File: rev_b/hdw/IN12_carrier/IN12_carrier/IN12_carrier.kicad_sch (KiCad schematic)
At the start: 0 parts

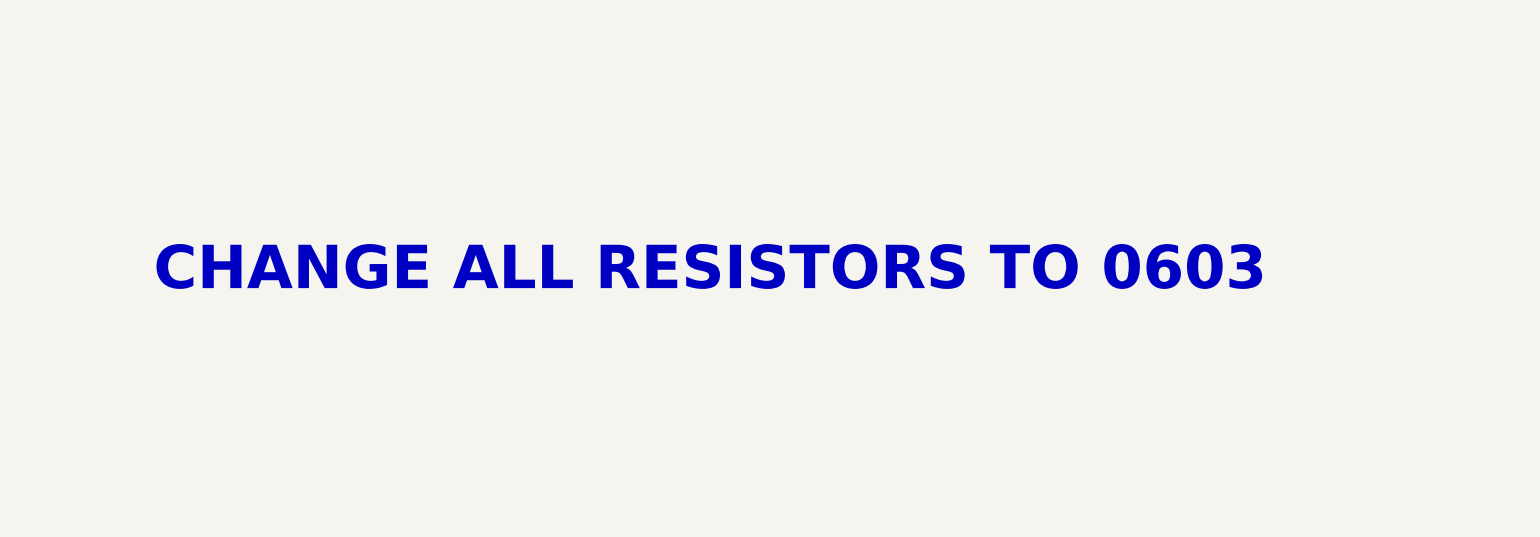
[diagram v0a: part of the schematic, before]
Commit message: updated footprints, ran some DRC
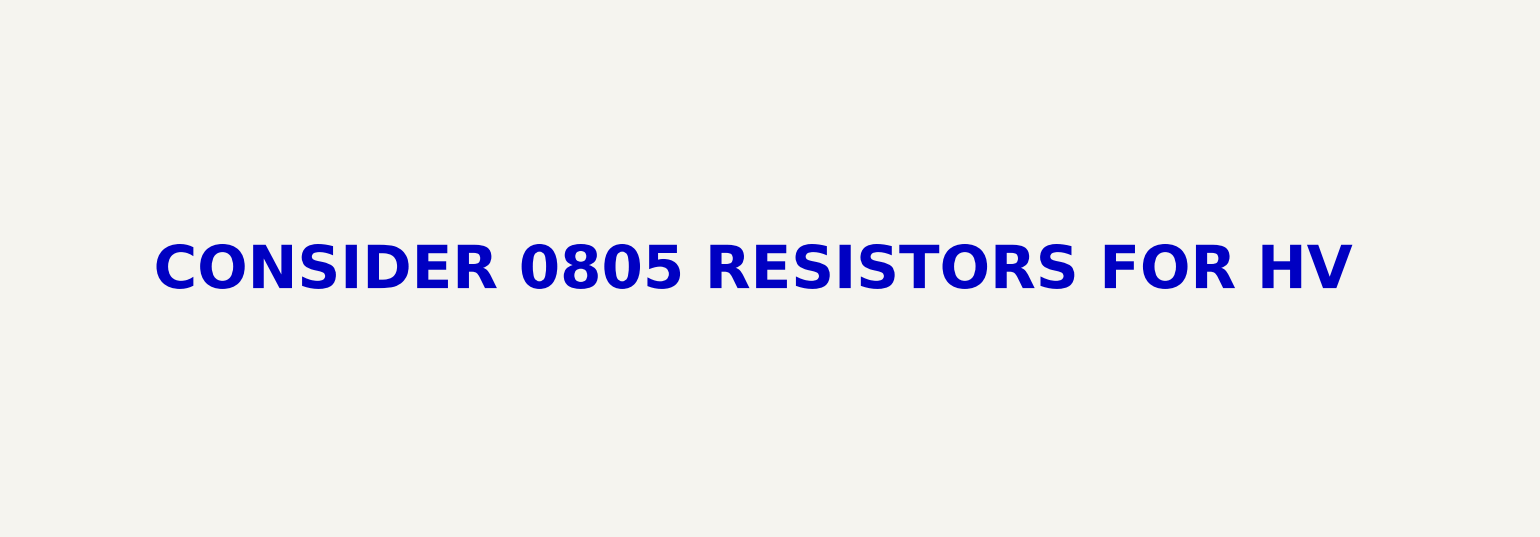
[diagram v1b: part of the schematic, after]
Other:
- note added: "CONSIDER 0805 RESISTORS FOR HV"
- note removed: "CHANGE ALL RESISTORS TO 0603"
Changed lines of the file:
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@@
     (company "Drew Maatman")
   )
-  (text "CHANGE ALL RESISTORS TO 0603" (at 121.92 52.07 0)
+  (text "CONSIDER 0805 RESISTORS FOR HV" (at 121.92 52.07 0)
     (effects (font (face "Courier New") (size 5.08 5.08) (thickness 1.016) bold (color 194 0 0 1)) (justify left bottom))
   )

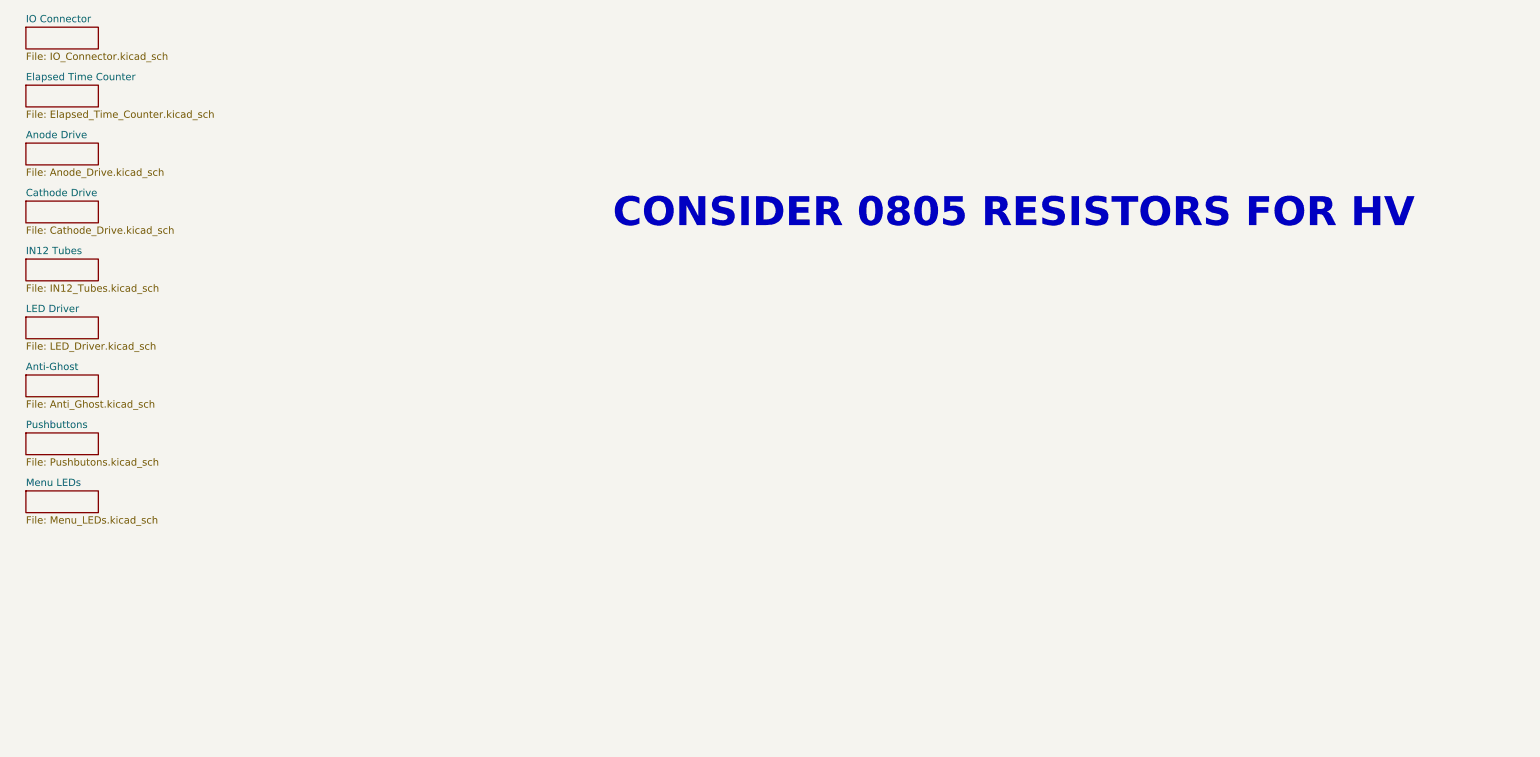
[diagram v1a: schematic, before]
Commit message: annotated, started arranging parts for IN12 carrier
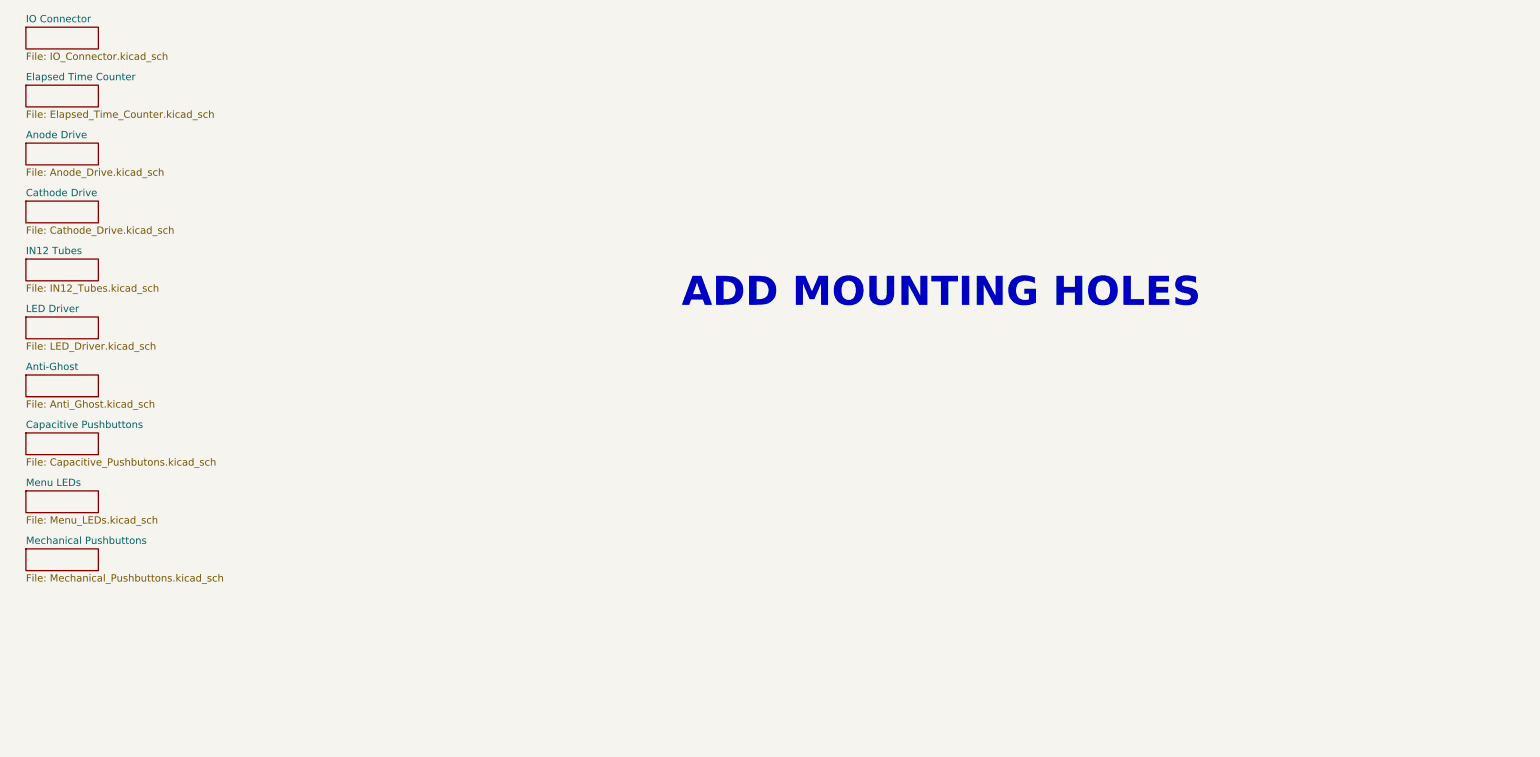
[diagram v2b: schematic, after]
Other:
- sheet Pushbuttons renamed Capacitive Pushbuttons
- added sheet Mechanical Pushbuttons (Mechanical_Pushbuttons.kicad_sch)
- sheet Capacitive Pushbuttons: file Pushbutons.kicad_sch -> Capacitive_Pushbutons.kicad_sch
- note added: "ADD MOUNTING HOLES"
- note removed: "CONSIDER 0805 RESISTORS FOR HV"
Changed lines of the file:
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@@
     (company "Drew Maatman")
   )
-  (text "CONSIDER 0805 RESISTORS FOR HV" (at 121.92 52.07 0)
-    (effects (font (face "Courier New") (size 5.08 5.08) (thickness 1.016) bold (color 194 0 0 1)) (justify left bottom))
+  (text "ADD MOUNTING HOLES" (at 133.985 66.04 0)
+    (effects (font (face "Courier New") (size 5.08 5.08) (thickness 1.016) bold (color 255 0 0 1)) (justify left bottom))
   )
   (sheet (at 19.05 46.99) (size 12.7 3.81) (fields_autoplaced)
@@
     (stroke (width 0.1524) (type solid))
     (fill (color 0 0 0 0.0000))
-    (property "Sheetname" "Pushbuttons" (at 19.05 86.9184 0)
+    (property "Sheetname" "Capacitive Pushbuttons" (at 19.05 86.9184 0)
       (effects (font (size 1.27 1.27)) (justify left bottom))
     )
-    (property "Sheetfile" "Pushbutons.kicad_sch" (at 19.05 92.0246 0)
+    (property "Sheetfile" "Capacitive_Pushbutons.kicad_sch" (at 19.05 92.0246 0)
       (effects (font (size 1.27 1.27)) (justify left top))
     )
@@
       )
     )
+  )
+  (sheet (at 19.05 107.95) (size 12.7 3.81) (fields_autoplaced)
+    (stroke (width 0.1524) (type solid))
+    (fill (color 0 0 0 0.0000))
+    (property "Sheetname" "Mechanical Pushbuttons" (at 19.05 107.2384 0)
+      (effects (font (size 1.27 1.27)) (justify left bottom))
+    )
+    (property "Sheetfile" "Mechanical_Pushbuttons.kicad_sch" (at 19.05 112.3446 0)
+      (effects (font (size 1.27 1.27)) (justify left top))
+    )
+    (instances
+      (project "IN12_carrier"
+        (path "/c4d83a5b-e6ae-4326-9df5-0c4ac01f7d8c" (page "11"))
+      )
+    )

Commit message: lots of placement progress on IN12 carrier board
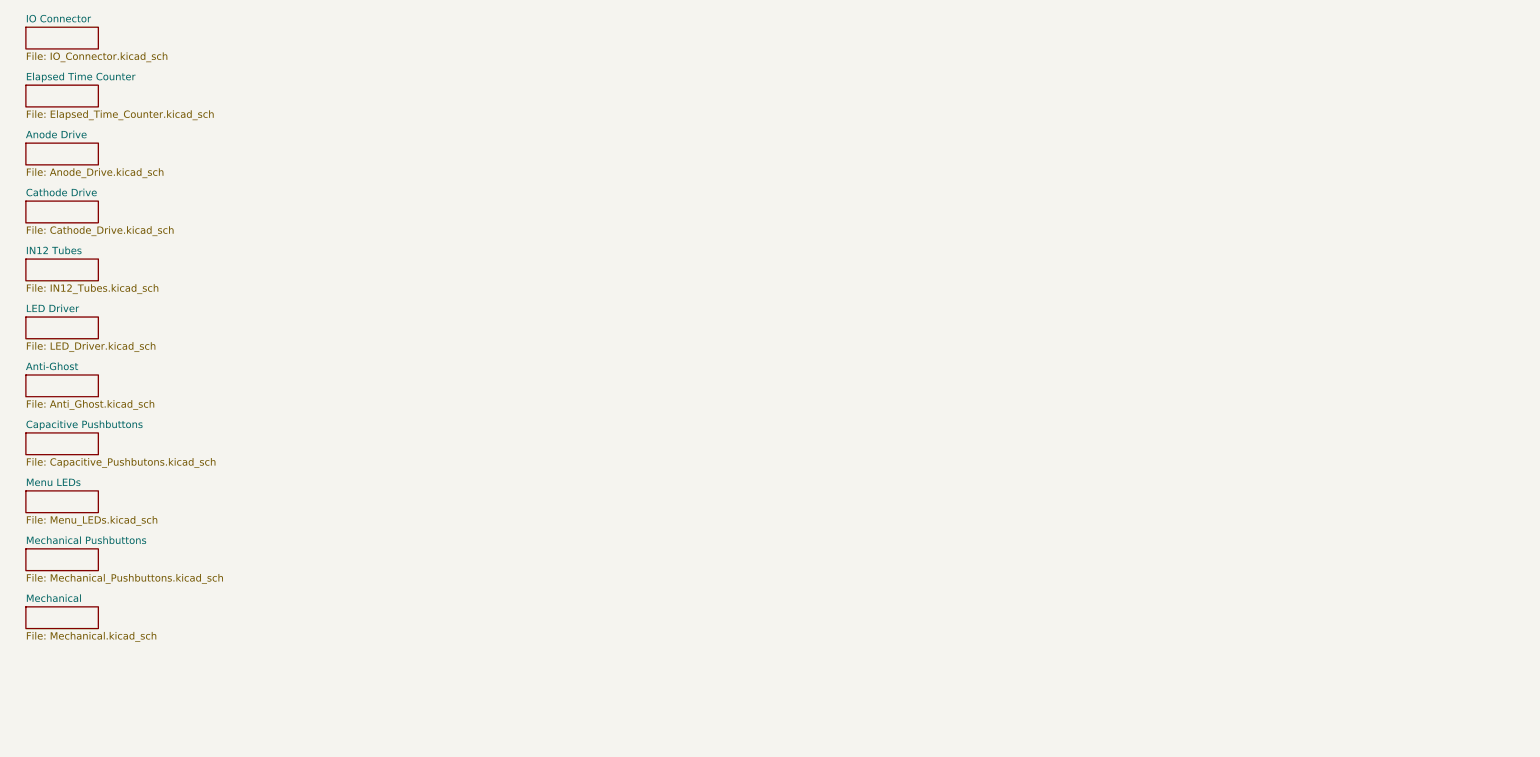
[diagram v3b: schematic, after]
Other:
- added sheet Mechanical (Mechanical.kicad_sch)
- note removed: "ADD MOUNTING HOLES"
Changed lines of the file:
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@@
     (company "Drew Maatman")
-  )
-  (text "ADD MOUNTING HOLES" (at 133.985 66.04 0)
-    (effects (font (face "Courier New") (size 5.08 5.08) (thickness 1.016) bold (color 255 0 0 1)) (justify left bottom))
   )
   (sheet (at 19.05 46.99) (size 12.7 3.81) (fields_autoplaced)
@@
       )
     )
+  )
+  (sheet (at 19.05 118.11) (size 12.7 3.81) (fields_autoplaced)
+    (stroke (width 0.1524) (type solid))
+    (fill (color 0 0 0 0.0000))
+    (property "Sheetname" "Mechanical" (at 19.05 117.3984 0)
+      (effects (font (size 1.27 1.27)) (justify left bottom))
+    )
+    (property "Sheetfile" "Mechanical.kicad_sch" (at 19.05 122.5046 0)
+      (effects (font (size 1.27 1.27)) (justify left top))
+    )
+    (instances
+      (project "IN12_carrier"
+        (path "/c4d83a5b-e6ae-4326-9df5-0c4ac01f7d8c" (page "12"))
+      )
+    )

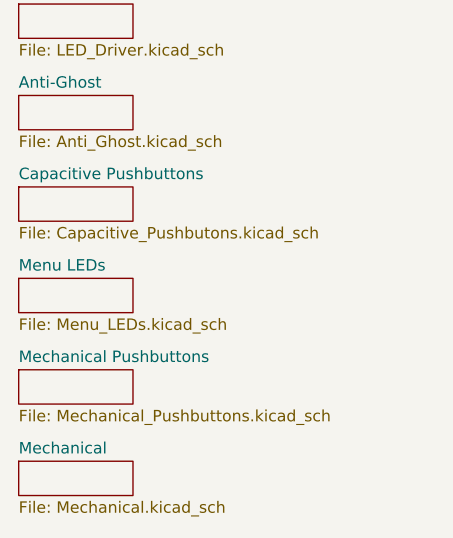
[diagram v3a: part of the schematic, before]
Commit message: lots of routing and design progress on IN12 carrier board
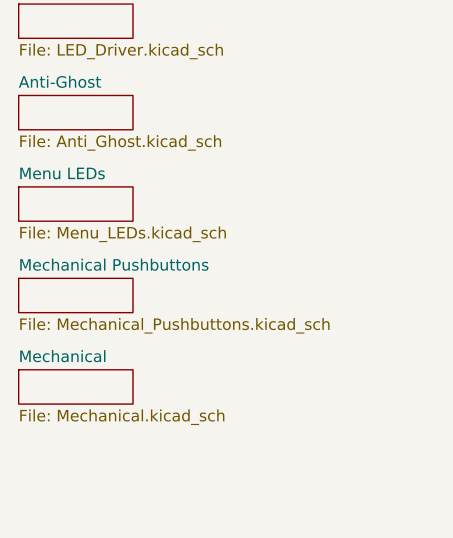
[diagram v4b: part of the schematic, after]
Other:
- removed sheet Capacitive Pushbuttons
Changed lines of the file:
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@@
     )
   )
-  (sheet (at 19.05 118.11) (size 12.7 3.81) (fields_autoplaced)
+  (sheet (at 19.05 107.95) (size 12.7 3.81) (fields_autoplaced)
     (stroke (width 0.1524) (type solid))
     (fill (color 0 0 0 0.0000))
-    (property "Sheetname" "Mechanical" (at 19.05 117.3984 0)
+    (property "Sheetname" "Mechanical" (at 19.05 107.2384 0)
       (effects (font (size 1.27 1.27)) (justify left bottom))
     )
-    (property "Sheetfile" "Mechanical.kicad_sch" (at 19.05 122.5046 0)
+    (property "Sheetfile" "Mechanical.kicad_sch" (at 19.05 112.3446 0)
       (effects (font (size 1.27 1.27)) (justify left top))
     )
@@
     )
   )
-  (sheet (at 19.05 97.79) (size 12.7 3.81) (fields_autoplaced)
+  (sheet (at 19.05 87.63) (size 12.7 3.81) (fields_autoplaced)
     (stroke (width 0.1524) (type solid))
     (fill (color 0 0 0 0.0000))
-    (property "Sheetname" "Menu LEDs" (at 19.05 97.0784 0)
+    (property "Sheetname" "Menu LEDs" (at 19.05 86.9184 0)
       (effects (font (size 1.27 1.27)) (justify left bottom))
     )
-    (property "Sheetfile" "Menu_LEDs.kicad_sch" (at 19.05 102.1846 0)
+    (property "Sheetfile" "Menu_LEDs.kicad_sch" (at 19.05 92.0246 0)
       (effects (font (size 1.27 1.27)) (justify left top))
     )
@@
     )
   )
-  (sheet (at 19.05 87.63) (size 12.7 3.81) (fields_autoplaced)
-    (stroke (width 0.1524) (type solid))
-    (fill (color 0 0 0 0.0000))
-    (property "Sheetname" "Capacitive Pushbuttons" (at 19.05 86.9184 0)
-      (effects (font (size 1.27 1.27)) (justify left bottom))
-    )
-    (property "Sheetfile" "Capacitive_Pushbutons.kicad_sch" (at 19.05 92.0246 0)
-      (effects (font (size 1.27 1.27)) (justify left top))
-    )
-    (instances
-      (project "IN12_carrier"
-        (path "/c4d83a5b-e6ae-4326-9df5-0c4ac01f7d8c" (page "9"))
-      )
-    )
-  )
   (sheet (at 19.05 67.31) (size 12.7 3.81) (fields_autoplaced)
     (stroke (width 0.1524) (type solid))
@@
     )
   )
-  (sheet (at 19.05 107.95) (size 12.7 3.81) (fields_autoplaced)
+  (sheet (at 19.05 97.79) (size 12.7 3.81) (fields_autoplaced)
     (stroke (width 0.1524) (type solid))
     (fill (color 0 0 0 0.0000))
-    (property "Sheetname" "Mechanical Pushbuttons" (at 19.05 107.2384 0)
+    (property "Sheetname" "Mechanical Pushbuttons" (at 19.05 97.0784 0)
       (effects (font (size 1.27 1.27)) (justify left bottom))
     )
-    (property "Sheetfile" "Mechanical_Pushbuttons.kicad_sch" (at 19.05 112.3446 0)
+    (property "Sheetfile" "Mechanical_Pushbuttons.kicad_sch" (at 19.05 102.1846 0)
       (effects (font (size 1.27 1.27)) (justify left top))
     )

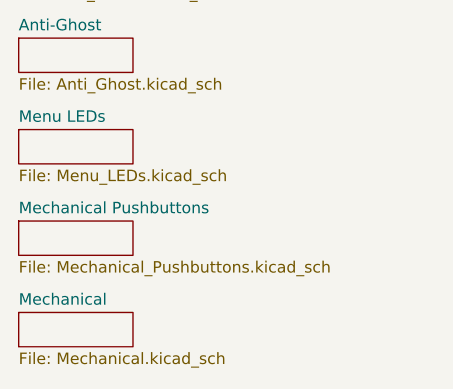
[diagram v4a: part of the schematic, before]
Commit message: added cap touch sensors back
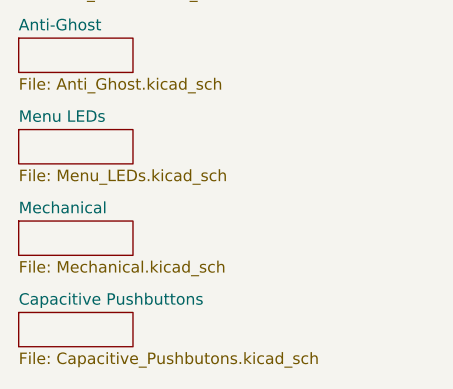
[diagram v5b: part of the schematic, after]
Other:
- removed sheet Mechanical Pushbuttons
- added sheet Capacitive Pushbuttons (Capacitive_Pushbutons.kicad_sch)
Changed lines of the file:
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@@
     (company "Drew Maatman")
+  )
+  (sheet (at 19.05 107.95) (size 12.7 3.81) (fields_autoplaced)
+    (stroke (width 0.1524) (type solid))
+    (fill (color 0 0 0 0.0000))
+    (property "Sheetname" "Capacitive Pushbuttons" (at 19.05 107.2384 0)
+      (effects (font (size 1.27 1.27)) (justify left bottom))
+    )
+    (property "Sheetfile" "Capacitive_Pushbutons.kicad_sch" (at 19.05 112.3446 0)
+      (effects (font (size 1.27 1.27)) (justify left top))
+    )
+    (instances
+      (project "IN12_carrier"
+        (path "/c4d83a5b-e6ae-4326-9df5-0c4ac01f7d8c" (page "11"))
+      )
+    )
   )
   (sheet (at 19.05 46.99) (size 12.7 3.81) (fields_autoplaced)
@@
     )
   )
-  (sheet (at 19.05 107.95) (size 12.7 3.81) (fields_autoplaced)
+  (sheet (at 19.05 97.79) (size 12.7 3.81) (fields_autoplaced)
     (stroke (width 0.1524) (type solid))
     (fill (color 0 0 0 0.0000))
-    (property "Sheetname" "Mechanical" (at 19.05 107.2384 0)
+    (property "Sheetname" "Mechanical" (at 19.05 97.0784 0)
       (effects (font (size 1.27 1.27)) (justify left bottom))
     )
-    (property "Sheetfile" "Mechanical.kicad_sch" (at 19.05 112.3446 0)
+    (property "Sheetfile" "Mechanical.kicad_sch" (at 19.05 102.1846 0)
       (effects (font (size 1.27 1.27)) (justify left top))
     )
@@
       )
     )
-  )
-  (sheet (at 19.05 97.79) (size 12.7 3.81) (fields_autoplaced)
-    (stroke (width 0.1524) (type solid))
-    (fill (color 0 0 0 0.0000))
-    (property "Sheetname" "Mechanical Pushbuttons" (at 19.05 97.0784 0)
-      (effects (font (size 1.27 1.27)) (justify left bottom))
-    )
-    (property "Sheetfile" "Mechanical_Pushbuttons.kicad_sch" (at 19.05 102.1846 0)
-      (effects (font (size 1.27 1.27)) (justify left top))
-    )
-    (instances
-      (project "IN12_carrier"
-        (path "/c4d83a5b-e6ae-4326-9df5-0c4ac01f7d8c" (page "11"))
-      )
-    )
